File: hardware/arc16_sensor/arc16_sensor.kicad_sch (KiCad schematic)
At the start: 1 part, among them U1 74HC4067

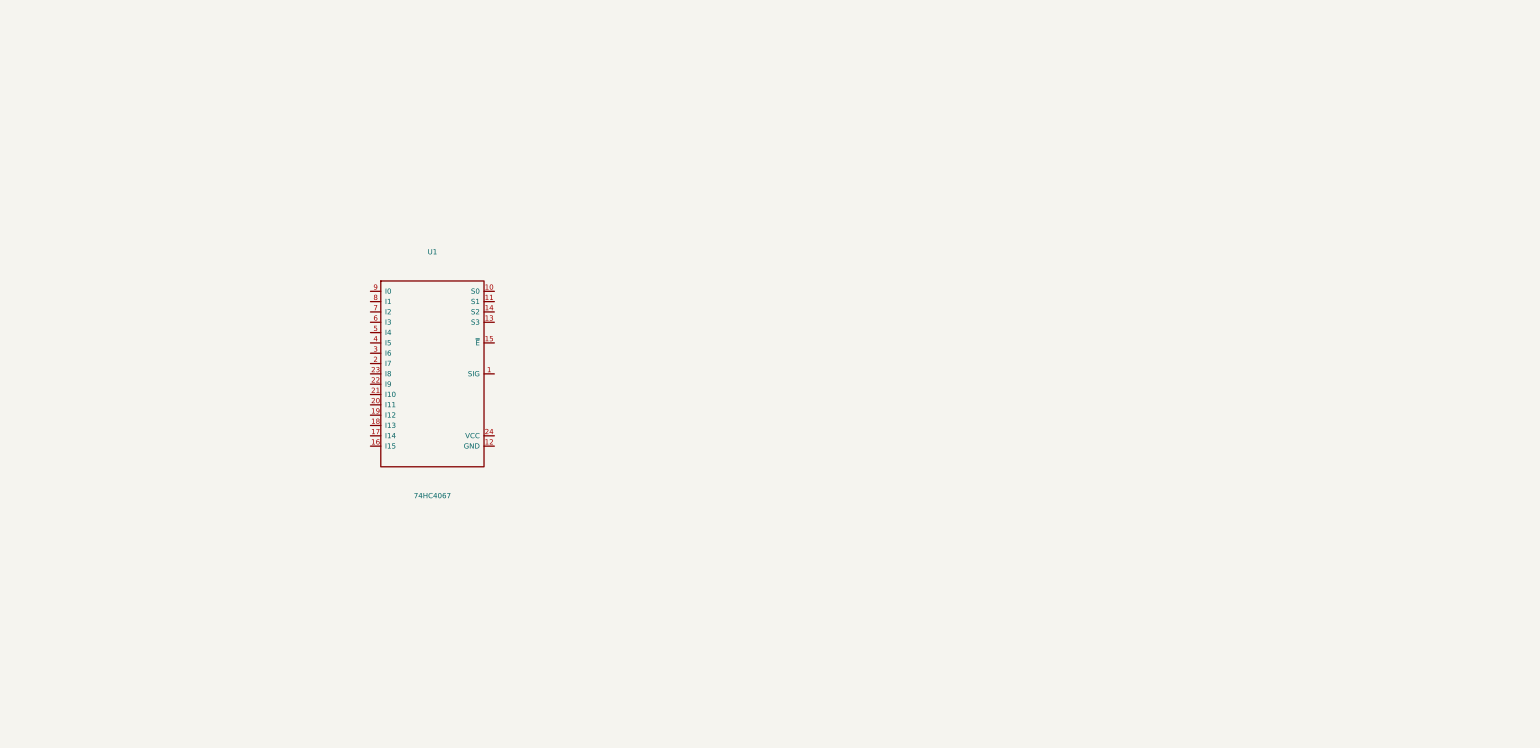
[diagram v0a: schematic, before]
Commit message: hardware: complete ARC16 schematic with all 16 IR LEDs, phototransistors, resistors, and MUX connections
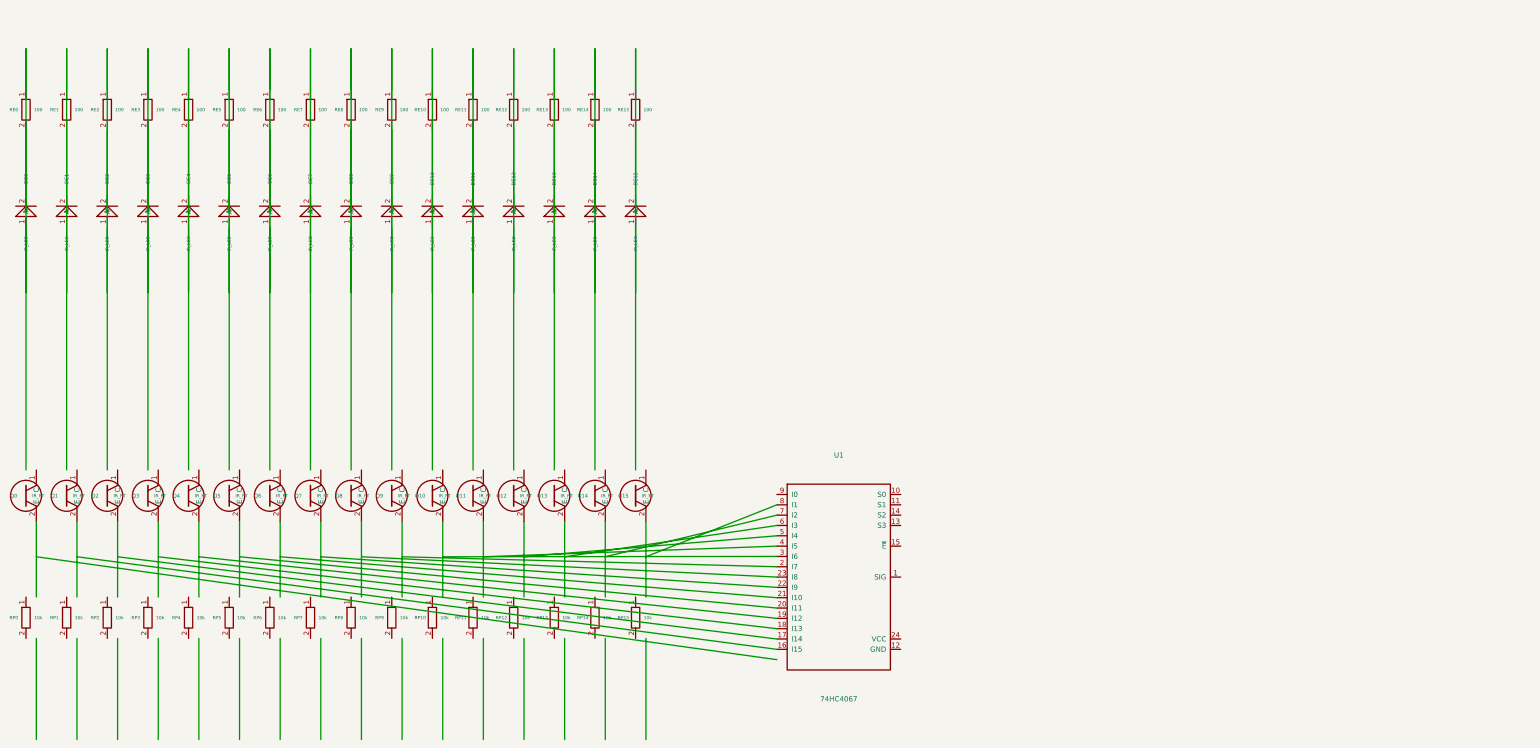
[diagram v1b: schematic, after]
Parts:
- added DE0, DE1, DE10, DE11, DE12, DE13, DE14, DE15, DE2, DE3, DE4, DE5, DE6, DE7, DE8, DE9: IR_LED, symbol Device:LED_IR
- added Q0, Q1, Q10, Q11, Q12, Q13, Q14, Q15, Q2, Q3, Q4, Q5, Q6, Q7, Q8, Q9: IR_PT, symbol Device:Q_Phototransistor_NPN
- added RE0, RE1, RE10, RE11, RE12, RE13, RE14, RE15, RE2, RE3, RE4, RE5, RE6, RE7, RE8, RE9: 100, symbol Device:R
- added RP0, RP1, RP10, RP11, RP12, RP13, RP14, RP15, RP2, RP3, RP4, RP5, RP6, RP7, RP8, RP9: 10k, symbol Device:R
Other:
- title: ARC16 - 16-Channel 2D Analog IR Sensor Array -> ARC16 - 16-Channel 2D Analog IR Reflectance Sensor Array
- moved on the sheet: U1

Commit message: hardware: clean visual schematic layout with net-label architecture for ARC16 16-channel array
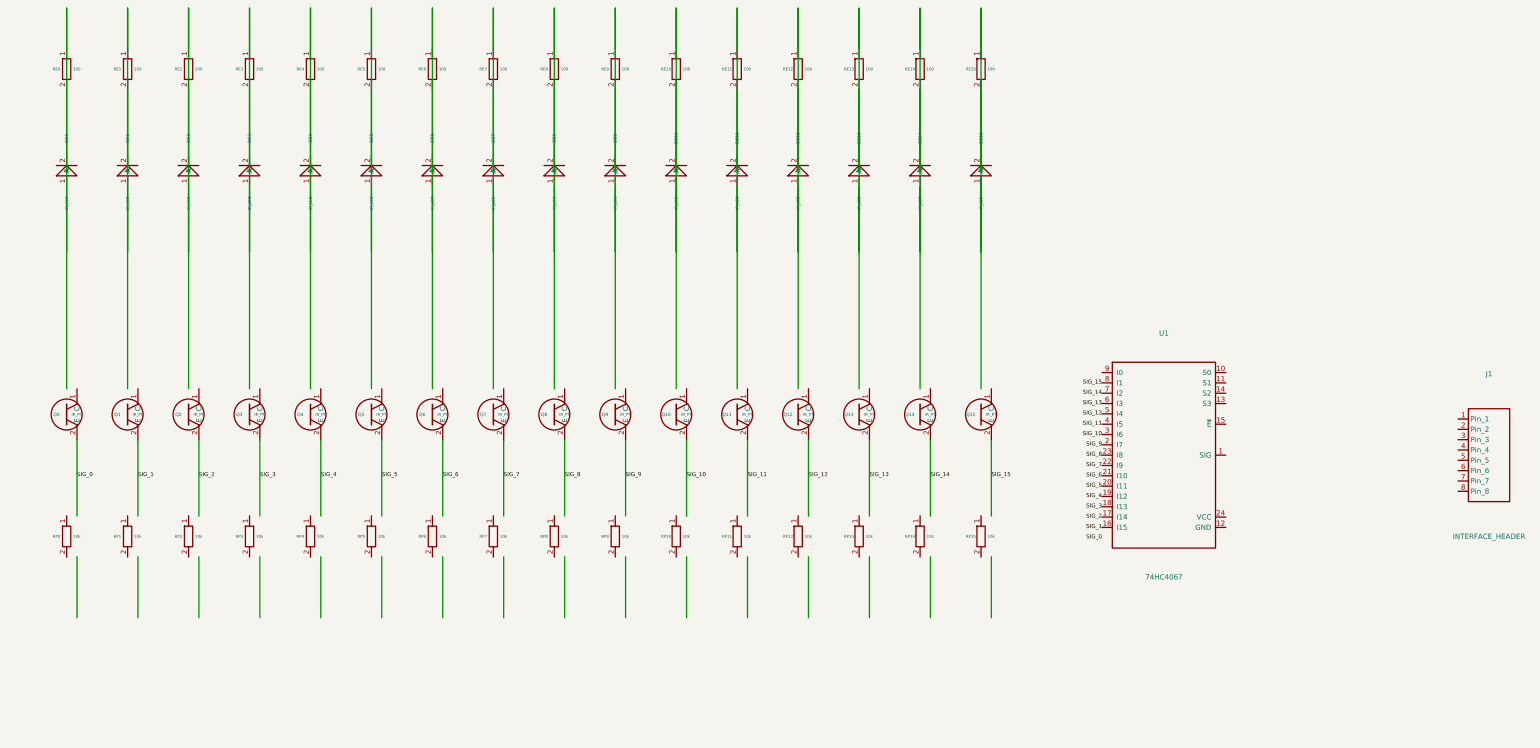
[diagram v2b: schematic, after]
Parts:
- added J1: INTERFACE_HEADER, symbol Connector:Conn_01x08_Pin
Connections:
- net SIG_0: now reaches Q0.2 (E)
- net SIG_1: now reaches Q1.2 (E)
- net SIG_1: now also U1.16 (I15)
- net SIG_2: now reaches Q2.2 (E)
- net SIG_2: now also U1.17 (I14)
- net SIG_3: now reaches Q3.2 (E)
- net SIG_3: now also U1.18 (I13)
- net SIG_4: now reaches Q4.2 (E)
- net SIG_4: now also U1.19 (I12)
- net SIG_5: now reaches Q5.2 (E)
- net SIG_5: now also U1.20 (I11)
- net SIG_6: now reaches Q6.2 (E)
- net SIG_6: now also U1.21 (I10)
- net SIG_7: now reaches Q7.2 (E)
- net SIG_7: now also U1.22 (I9)
- net SIG_8: now reaches Q8.2 (E)
- net SIG_8: now also U1.23 (I8)
- net SIG_9: now reaches Q9.2 (E)
- net SIG_9: now also U1.2 (I7)
- net SIG_10: now reaches Q10.2 (E)
- net SIG_10: now also U1.3 (I6)
- net SIG_11: now reaches Q11.2 (E)
- net SIG_11: now also U1.4 (I5)
- net SIG_12: now reaches Q12.2 (E)
- net SIG_12: now also U1.5 (I4)
- net SIG_13: now reaches Q13.2 (E)
- net SIG_13: now also U1.6 (I3)
- net SIG_14: now reaches Q14.2 (E)
- net SIG_14: now also U1.7 (I2)
- net SIG_15: now reaches Q15.2 (E)
- net SIG_15: now also U1.8 (I1)
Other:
- moved on the sheet: DE0, DE1, DE10, DE11, DE12, DE13, DE14, DE15, DE2, DE3, DE4, DE5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
